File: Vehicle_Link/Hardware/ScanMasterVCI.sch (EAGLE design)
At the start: 91 parts, among them IC1 XMEGA32A4U, Q1 MMBT4403, Q10 ZXMP6A17G, Q11 MMBT3904, Q12 MMBT3904, Q13 MMBT3904, Q2 MMBT3904, Q3 MMBT3904, Q4 MMBT3904, Q5 MMBT3904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

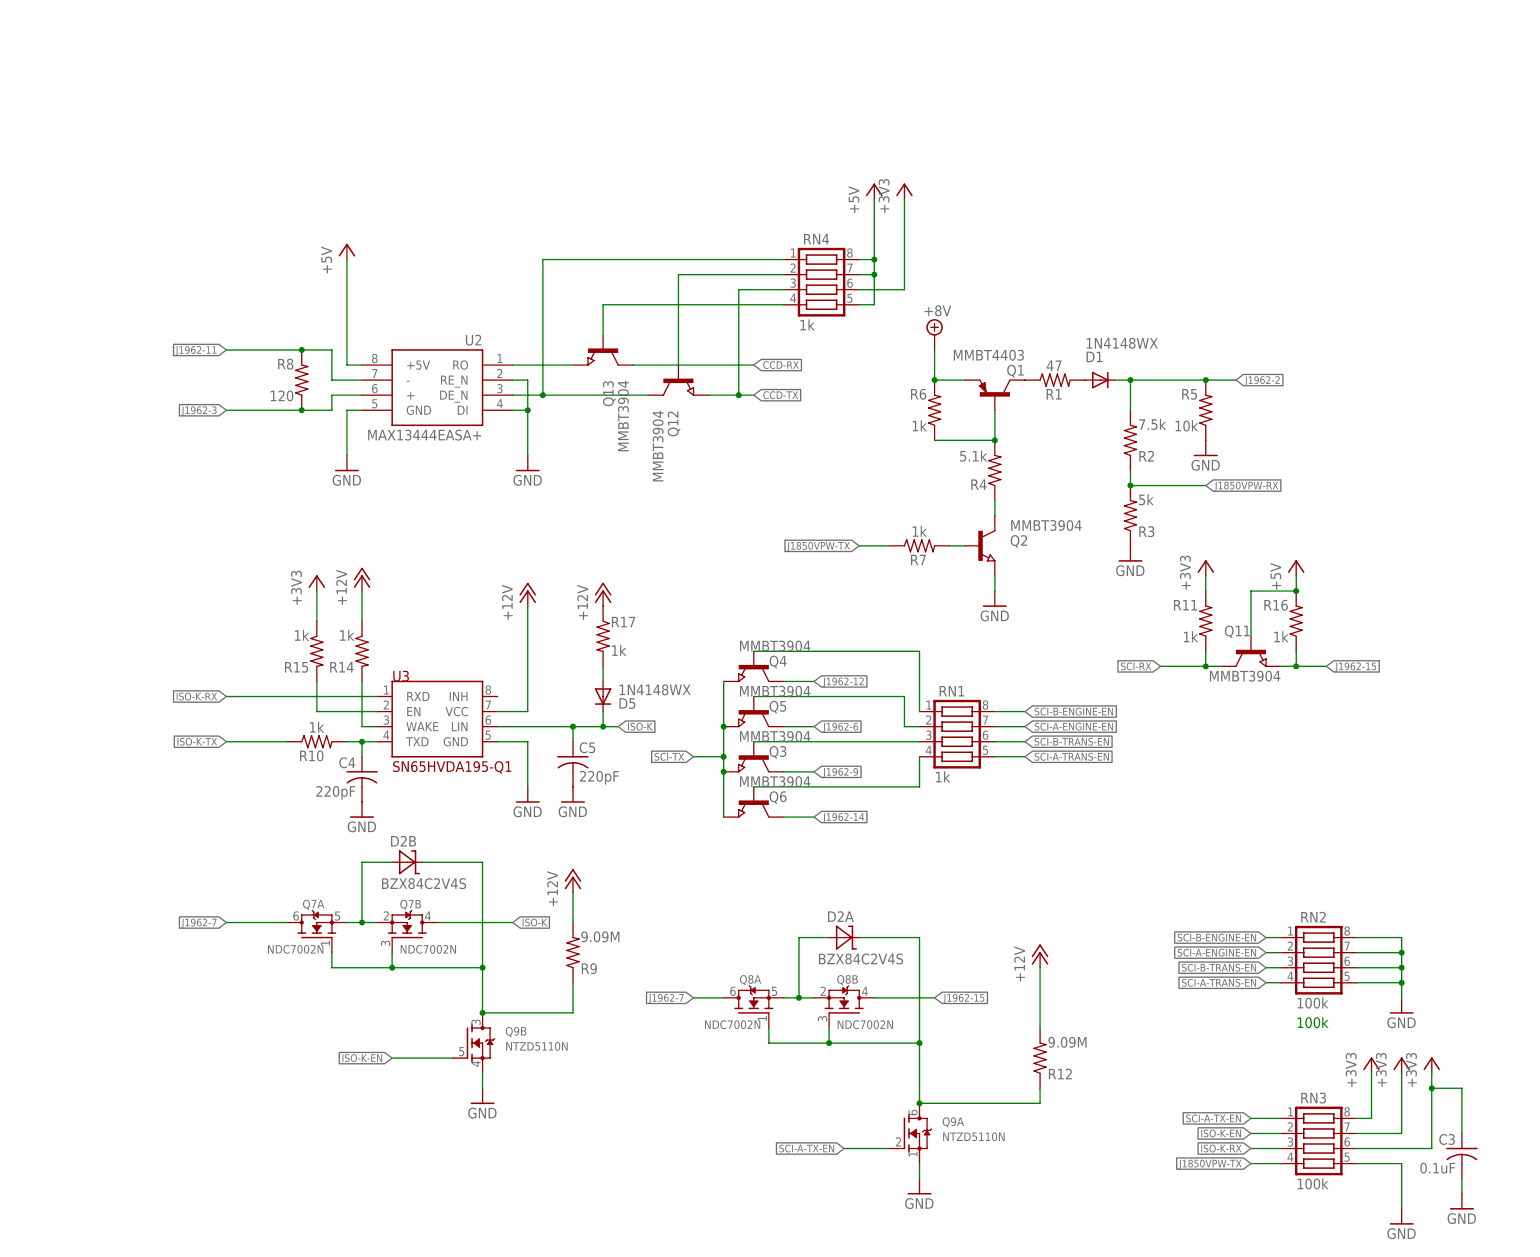
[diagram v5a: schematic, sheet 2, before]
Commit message: Deleted MOSFETs. They don't appear to work well with ISO9141. I need another way to switch between 5V/12V. Probably going to switch to simple transistors.
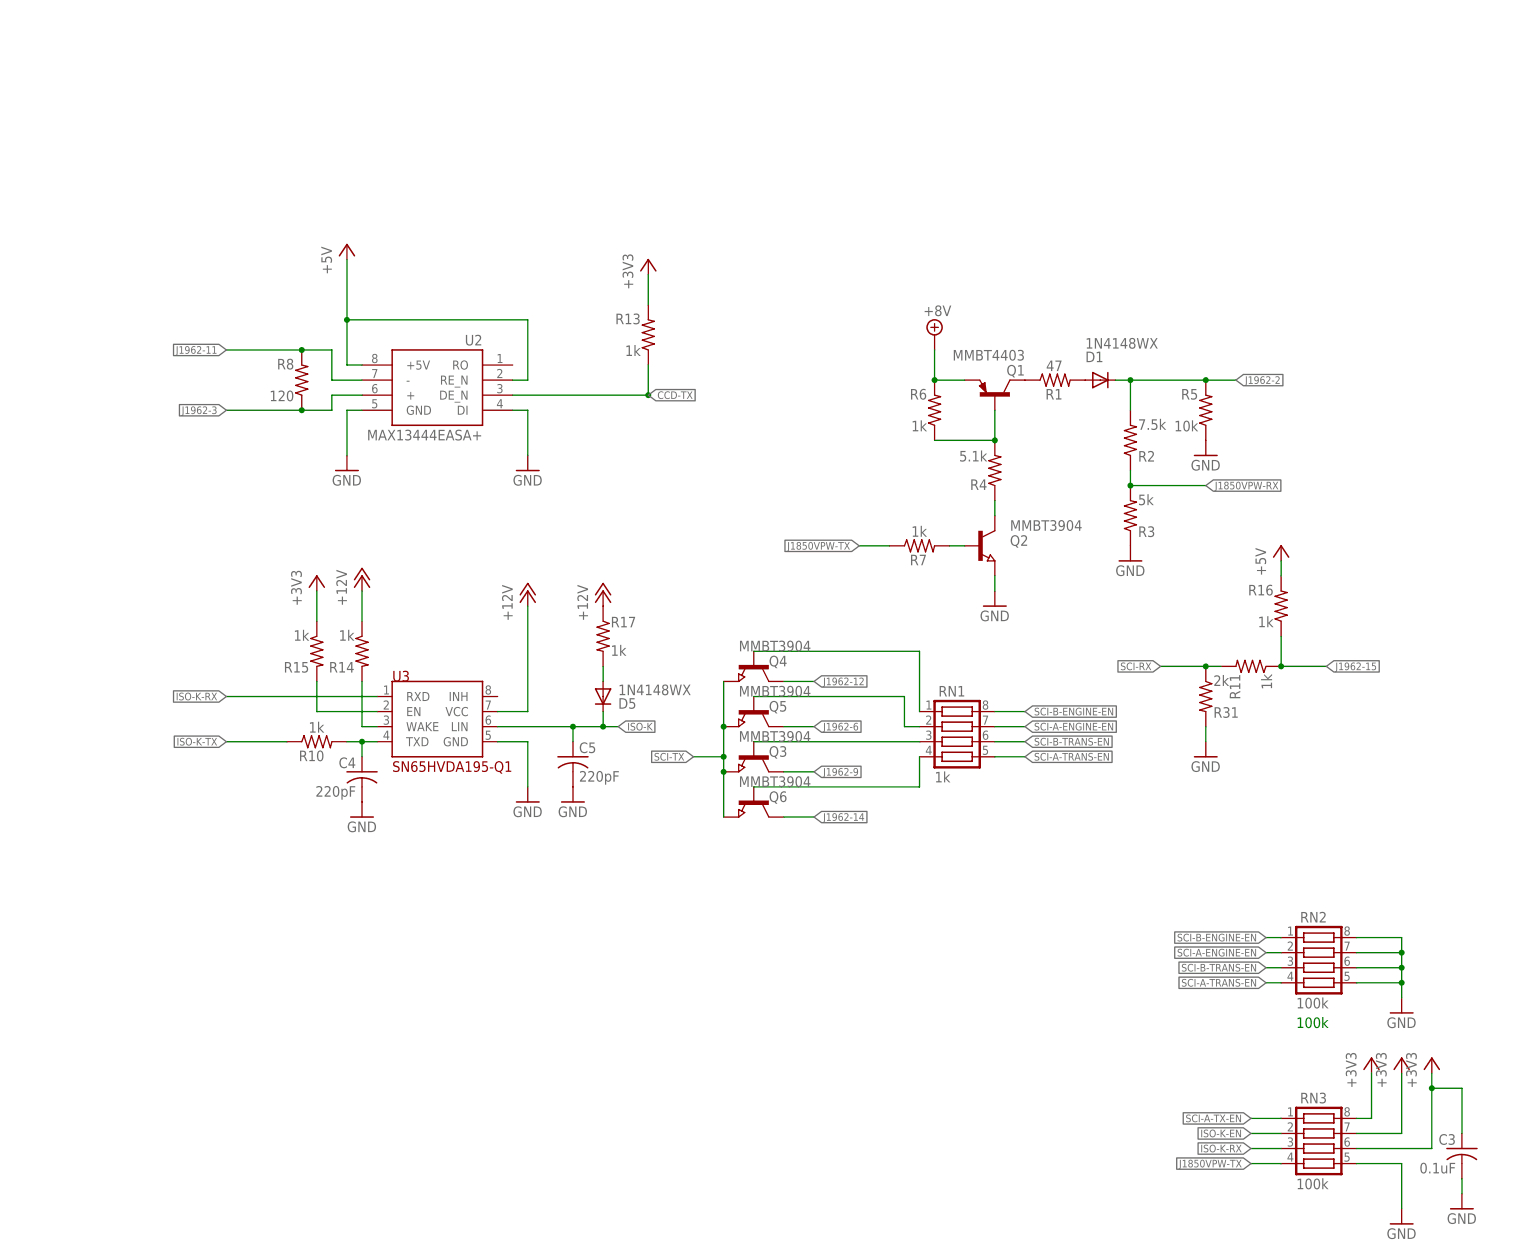
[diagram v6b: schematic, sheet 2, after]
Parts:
- removed D2: BZX84C2V4S, customics:BZX84C2V4S
- removed Q11, Q12, Q13: MMBT3904, semicon-smd-ipc:NPN-TRANSISTOR_SOT23
- removed Q7, Q8: NDC7002N, customics:NDC7002N
- removed Q9: NTZD5110N, customics:NTZD5110N
- removed R12, R9: 9.09M, adafruit:R-US_R0603
- removed RN4: 1k, resistor-net:CTS742C083
- added R13: 1k, adafruit:R-US_R0603
- added R31: 2k, adafruit:R-US_R0603
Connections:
- removed net N$1: D2A.A, Q8A.S, Q8B.S
- removed net N$11: D2B.C, Q7A.G, Q7B.G, Q9B.D, R9.1
- removed net N$32: Q12.C, RN4.1, U2.DE_N
- removed net N$33: Q12.B, RN4.2
- removed net N$34: Q13.E, U2.RO
- removed net N$35: Q13.B, RN4.4
- removed net N$4: D2B.A, Q7A.S, Q7B.S
- removed net N$5: D2A.C, Q8A.G, Q8B.G, Q9A.D, R12.1
- net +12V: no longer R12.2, R9.2
- net +3V3: now also R13.2; no longer R11.2, RN4.6
- net +5V: now also U2.RE_N; no longer Q11.B, RN4.5, RN4.7, RN4.8
- net CCD-RX: no longer Q13.C
- net CCD-TX: now also R13.1, U2.DE_N; no longer Q12.E, RN4.3
- net GND: now also R31.2; no longer Q9A.S, Q9B.S, U2.RE_N
- net ISO-K: no longer Q7B.D
- net ISO-K-EN: no longer Q9B.G
- net J1962-15: now also R11.1; no longer Q11.E, Q8B.D
- net J1962-7: no longer Q7A.D, Q8A.D
- net SCI-A-TX-EN: no longer Q9A.G
- net SCI-RX: now also R11.2, R31.1; no longer Q11.C, R11.1
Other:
- moved on the sheet: R11, R16

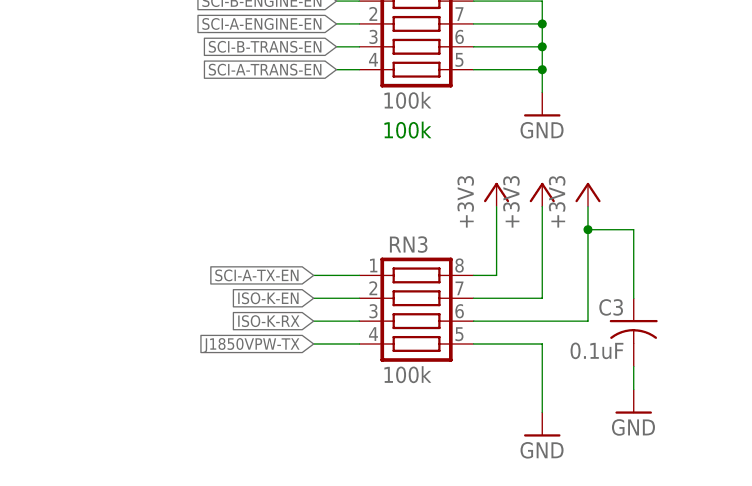
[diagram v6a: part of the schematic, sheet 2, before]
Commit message: Re-ran a few more data traces for style. Laid out everything on the board with latest schematic.
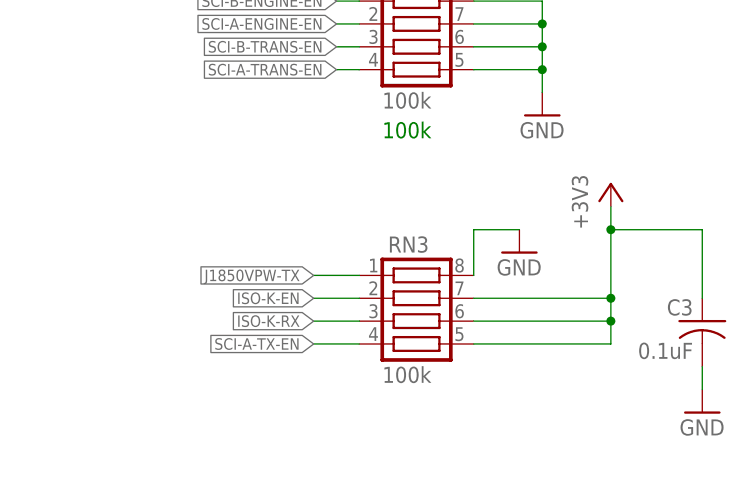
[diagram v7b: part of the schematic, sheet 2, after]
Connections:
- net +3V3: now also RN3.5; no longer RN3.8
- net GND: now also RN3.8; no longer RN3.5
- net J1850VPW-TX: now also RN3.1; no longer RN3.4
- net SCI-A-TX-EN: now also RN3.4; no longer RN3.1
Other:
- moved on the sheet: C3
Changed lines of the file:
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@@
 <part name="P12" library="pinhead" library_urn="urn:adsk.eagle:library:325" deviceset="PINHD-1X1" device="" package3d_urn="urn:adsk.eagle:package:22485/1"/>
 <part name="RN3" library="resistor-net" library_urn="urn:adsk.eagle:library:343" deviceset="CTS742C083" device="" package3d_urn="urn:adsk.eagle:package:24985/1" value="100k"/>
-<part name="GND37" library="supply1" library_urn="urn:adsk.eagle:library:371" deviceset="GND" device=""/>
-<part name="+3V9" library="supply1" library_urn="urn:adsk.eagle:library:371" deviceset="+3V3" device=""/>
-<part name="+3V10" library="supply1" library_urn="urn:adsk.eagle:library:371" deviceset="+3V3" device=""/>
 <part name="+3V6" library="supply1" library_urn="urn:adsk.eagle:library:371" deviceset="+3V3" device=""/>
 <part name="C3" library="adafruit" library_urn="urn:adsk.eagle:library:420" deviceset="C-US" device="C0603" value="0.1uF"/>
@@
 <part name="R31" library="adafruit" library_urn="urn:adsk.eagle:library:420" deviceset="R-US_" device="R0603" value="2k"/>
 <part name="GND5" library="supply1" library_urn="urn:adsk.eagle:library:371" deviceset="GND" device=""/>
+<part name="GND6" library="supply1" library_urn="urn:adsk.eagle:library:371" deviceset="GND" device=""/>
 </parts>
 <sheets>
@@
 <instance part="RN1" gate="G$1" x="132.08" y="139.7"/>
 <instance part="RN3" gate="G$1" x="193.04" y="71.12"/>
-<instance part="GND37" gate="1" x="208.28" y="55.88"/>
-<instance part="+3V9" gate="G$1" x="203.2" y="83.82"/>
-<instance part="+3V10" gate="G$1" x="208.28" y="83.82"/>
-<instance part="+3V6" gate="G$1" x="213.36" y="83.82"/>
-<instance part="C3" gate="G$1" x="218.44" y="68.58" rot="MR0"/>
-<instance part="GND42" gate="1" x="218.44" y="58.42"/>
+<instance part="+3V6" gate="G$1" x="215.9" y="83.82"/>
+<instance part="C3" gate="G$1" x="226.06" y="68.58" rot="MR0"/>
+<instance part="GND42" gate="1" x="226.06" y="58.42"/>
 <instance part="U2" gate="G$1" x="45.72" y="195.58" rot="MR0"/>
 <instance part="GND3" gate="1" x="60.96" y="182.88"/>
@@
 </instance>
 <instance part="GND5" gate="1" x="175.26" y="134.62"/>
+<instance part="GND6" gate="1" x="205.74" y="76.2"/>
 </instances>
 <busses>
@@
 </segment>
 <segment>
-<pinref part="RN3" gate="G$1" pin="8"/>
-<wire x1="200.66" y1="73.66" x2="203.2" y2="73.66" width="0.1524" layer="91"/>
-<wire x1="203.2" y1="73.66" x2="203.2" y2="81.28" width="0.1524" layer="91"/>
-<pinref part="+3V9" gate="G$1" pin="+3V3"/>
-</segment>
-<segment>
+<pinref part="RN3" gate="G$1" pin="6"/>
+<wire x1="200.66" y1="68.58" x2="215.9" y2="68.58" width="0.1524" layer="91"/>
+<wire x1="215.9" y1="68.58" x2="215.9" y2="71.12" width="0.1524" layer="91"/>
+<pinref part="+3V6" gate="G$1" pin="+3V3"/>
+<wire x1="215.9" y1="71.12" x2="215.9" y2="78.74" width="0.1524" layer="91"/>
+<wire x1="215.9" y1="78.74" x2="215.9" y2="81.28" width="0.1524" layer="91"/>
+<wire x1="215.9" y1="78.74" x2="226.06" y2="78.74" width="0.1524" layer="91"/>
+<junction x="215.9" y="78.74"/>
+<wire x1="226.06" y1="78.74" x2="226.06" y2="71.12" width="0.1524" layer="91"/>
+<pinref part="C3" gate="G$1" pin="1"/>
 <pinref part="RN3" gate="G$1" pin="7"/>
-<wire x1="200.66" y1="71.12" x2="208.28" y2="71.12" width="0.1524" layer="91"/>
-<wire x1="208.28" y1="71.12" x2="208.28" y2="81.28" width="0.1524" layer="91"/>
-<pinref part="+3V10" gate="G$1" pin="+3V3"/>
-</segment>
-<segment>
-<pinref part="RN3" gate="G$1" pin="6"/>
-<wire x1="200.66" y1="68.58" x2="213.36" y2="68.58" width="0.1524" layer="91"/>
-<wire x1="213.36" y1="68.58" x2="213.36" y2="78.74" width="0.1524" layer="91"/>
-<pinref part="+3V6" gate="G$1" pin="+3V3"/>
-<wire x1="213.36" y1="78.74" x2="213.36" y2="81.28" width="0.1524" layer="91"/>
-<wire x1="213.36" y1="78.74" x2="218.44" y2="78.74" width="0.1524" layer="91"/>
-<junction x="213.36" y="78.74"/>
-<wire x1="218.44" y1="78.74" x2="218.44" y2="71.12" width="0.1524" layer="91"/>
-<pinref part="C3" gate="G$1" pin="1"/>
+<wire x1="200.66" y1="71.12" x2="215.9" y2="71.12" width="0.1524" layer="91"/>
+<junction x="215.9" y="71.12"/>
+<pinref part="RN3" gate="G$1" pin="5"/>
+<wire x1="200.66" y1="66.04" x2="215.9" y2="66.04" width="0.1524" layer="91"/>
+<wire x1="215.9" y1="66.04" x2="215.9" y2="68.58" width="0.1524" layer="91"/>
+<junction x="215.9" y="68.58"/>
 </segment>
 <segment>
@@
 </segment>
 <segment>
-<pinref part="RN3" gate="G$1" pin="5"/>
-<wire x1="208.28" y1="66.04" x2="200.66" y2="66.04" width="0.1524" layer="91"/>
-<wire x1="208.28" y1="66.04" x2="208.28" y2="58.42" width="0.1524" layer="91"/>
-<pinref part="GND37" gate="1" pin="GND"/>
-</segment>
-<segment>
 <pinref part="C3" gate="G$1" pin="2"/>
 <pinref part="GND42" gate="1" pin="GND"/>
-<wire x1="218.44" y1="60.96" x2="218.44" y2="63.5" width="0.1524" layer="91"/>
+<wire x1="226.06" y1="60.96" x2="226.06" y2="63.5" width="0.1524" layer="91"/>
 </segment>
 <segment>
@@
 <pinref part="GND5" gate="1" pin="GND"/>
 <wire x1="175.26" y1="137.16" x2="175.26" y2="139.7" width="0.1524" layer="91"/>
+</segment>
+<segment>
+<pinref part="RN3" gate="G$1" pin="8"/>
+<wire x1="200.66" y1="73.66" x2="200.66" y2="78.74" width="0.1524" layer="91"/>
+<wire x1="200.66" y1="78.74" x2="205.74" y2="78.74" width="0.1524" layer="91"/>
+<pinref part="GND6" gate="1" pin="GND"/>
 </segment>
 </net>
@@
 </segment>
 <segment>
-<pinref part="RN3" gate="G$1" pin="4"/>
-<wire x1="182.88" y1="66.04" x2="187.96" y2="66.04" width="0.1524" layer="91"/>
-<label x="182.88" y="66.04" size="1.27" layer="95" rot="R180" xref="yes"/>
+<pinref part="RN3" gate="G$1" pin="1"/>
+<wire x1="187.96" y1="73.66" x2="182.88" y2="73.66" width="0.1524" layer="91"/>
+<label x="182.88" y="73.66" size="1.27" layer="95" rot="R180" xref="yes"/>
 </segment>
 </net>
@@
 </segment>
 </net>
-<net name="SCI-A-TX-EN" class="0">
-<segment>
-<pinref part="RN3" gate="G$1" pin="1"/>
-<wire x1="187.96" y1="73.66" x2="182.88" y2="73.66" width="0.1524" layer="91"/>
-<label x="182.88" y="73.66" size="1.27" layer="95" rot="R180" xref="yes"/>
-</segment>
-</net>
 <net name="SCI-RX" class="0">
 <segment>
@@
 </segment>
 </net>
+<net name="SCI-A-TX-EN" class="0">
+<segment>
+<pinref part="RN3" gate="G$1" pin="4"/>
+<wire x1="187.96" y1="66.04" x2="182.88" y2="66.04" width="0.1524" layer="91"/>
+<label x="182.88" y="66.04" size="1.27" layer="95" rot="R180" xref="yes"/>
+</segment>
+</net>
